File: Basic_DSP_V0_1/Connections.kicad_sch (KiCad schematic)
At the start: 40 parts, among them J10 53048-0310, J13 USB_C_Receptacle, J14 53048-0210, J15 53048-0210, J16 Conn_02x08_Odd_Even, J2 53048-0310, J3 53048-0310, J7 53048-0310, J8 53048-0310, J9 53048-0310

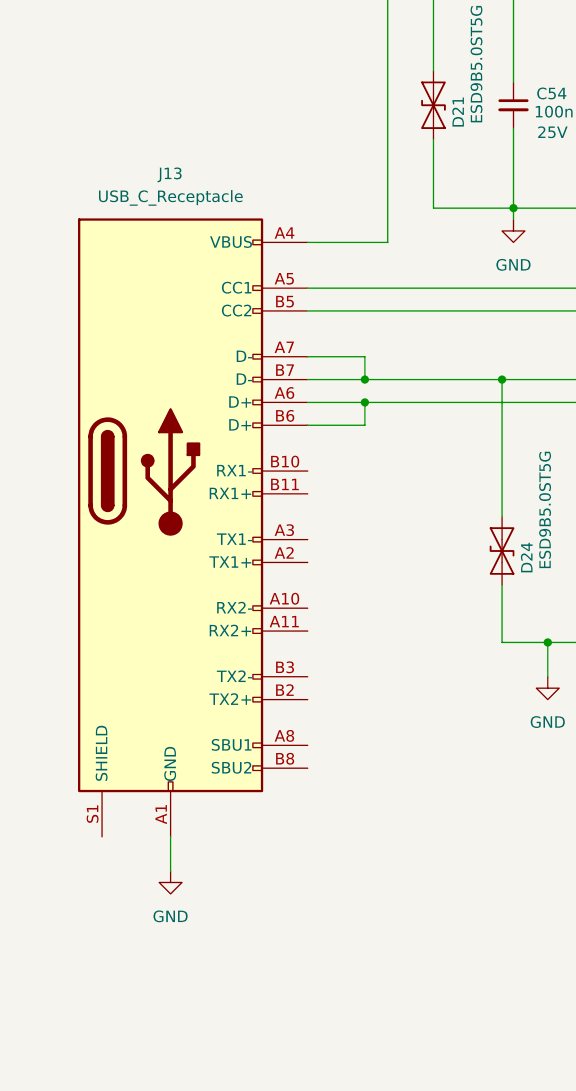
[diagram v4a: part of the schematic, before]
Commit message: More layout on Basic_DSP_V0_1 and a change of USB connector
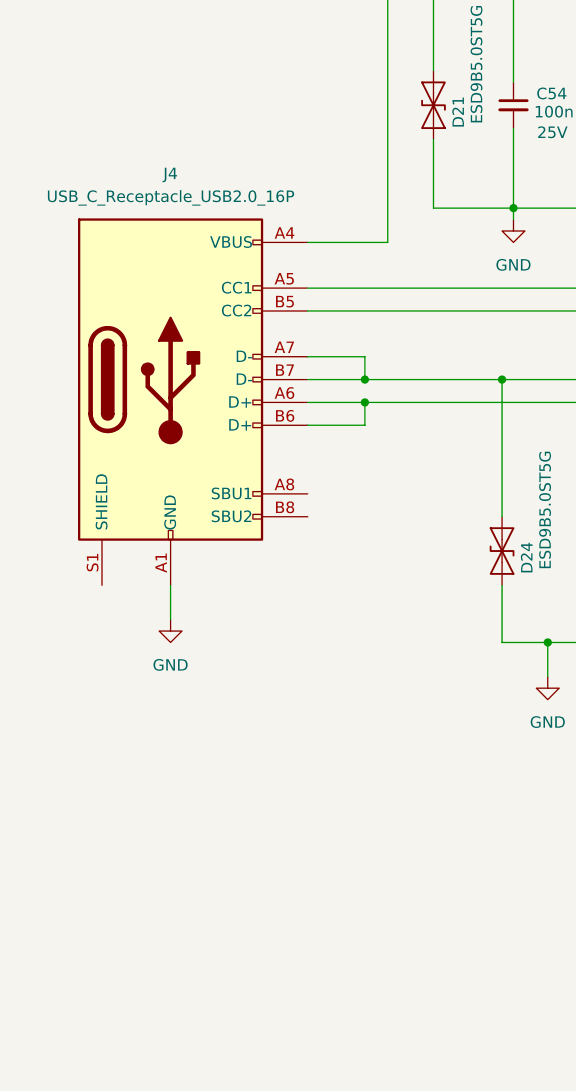
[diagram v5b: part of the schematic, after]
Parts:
- removed J13: USB_C_Receptacle, Connector_USB:USB_C_Receptacle_Molex_105450-0101, symbol Connector:USB_C_Receptacle
- added J4: USB_C_Receptacle_USB2.0_16P, Connector_USB:USB_C_Receptacle_GCT_USB4085, symbol Connector:USB_C_Receptacle_USB2.0_16P
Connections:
- net GND: now also J4.A1 (GND), J4.A12 (GND), J4.B1 (GND), J4.B12 (GND)
- net USB_D+: now also J4.A6 (D+), J4.B6 (D+)
- net USB_D-: now also J4.A7 (D-), J4.B7 (D-)
- net VBUS: now also J4.A4 (VBUS), J4.A9 (VBUS), J4.B4 (VBUS), J4.B9 (VBUS)
- net at R40.2: now also J4.A5 (CC1)
- net at R39.2: now also J4.B5 (CC2)
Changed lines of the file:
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@@
 	(wire
 		(pts
-			(xy 104.14 170.18) (xy 104.14 173.99)
+			(xy 104.14 142.24) (xy 104.14 146.05)
 		)
 		(stroke
@@
 	)
 	(symbol
+		(lib_id "Connector:USB_C_Receptacle_USB2.0_16P")
+		(at 104.14 119.38 0)
+		(unit 1)
+		(exclude_from_sim no)
+		(in_bom yes)
+		(on_board yes)
+		(dnp no)
+		(fields_autoplaced yes)
+		(property "Reference" "J4"
+			(at 104.14 96.52 0)
+			(effects
+				(font
+					(size 1.27 1.27)
+				)
+			)
+		)
+		(property "Value" "USB_C_Receptacle_USB2.0_16P"
+			(at 104.14 99.06 0)
+			(effects
+				(font
+					(size 1.27 1.27)
+				)
+			)
+		)
+		(property "Footprint" "Connector_USB:USB_C_Receptacle_GCT_USB4085"
+			(at 107.95 119.38 0)
+			(effects
+				(font
+					(size 1.27 1.27)
+				)
+				(hide yes)
+			)
+		)
+		(property "Datasheet" "https://www.usb.org/sites/default/files/documents/usb_type-c.zip"
+			(at 107.95 119.38 0)
+			(effects
+				(font
+					(size 1.27 1.27)
+				)
+				(hide yes)
+			)
+		)
+		(property "Description" "USB 2.0-only 16P Type-C Receptacle connector"
+			(at 104.14 119.38 0)
+			(effects
+				(font
+					(size 1.27 1.27)
+				)
+				(hide yes)
+			)
+		)
+		(pin "A4"
+		)
+		(pin "B7"
+		)
+		(pin "A12"
+		)
+		(pin "A7"
+		)
+		(pin "B5"
+		)
+		(pin "B8"
+		)
+		(pin "A8"
+		)
+		(pin "A9"
+		)
+		(pin "A5"
+		)
+		(pin "A1"
+		)
+		(pin "B12"
+		)
+		(pin "B4"
+		)
+		(pin "S1"
+		)
+		(pin "B1"
+		)
+		(pin "B6"
+		)
+		(pin "B9"
+		)
+		(pin "A6"
+		)
+		(instances
+			(project ""
+				(path "/b632011b-bebd-450c-b21c-a571983f756a/a6a37837-a89c-47bf-8760-dcad102ca010"
+					(reference "J4")
+					(unit 1)
+				)
+			)
+		)
+	)
+	(symbol
 		(lib_id "Chase_Conn:53048-0310")
 		(at 527.05 92.71 0)
@@
 	)
 	(symbol
-		(lib_id "Connector:USB_C_Receptacle")
-		(at 104.14 129.54 0)
-		(unit 1)
-		(exclude_from_sim no)
-		(in_bom yes)
-		(on_board yes)
-		(dnp no)
-		(fields_autoplaced yes)
-		(property "Reference" "J13"
-			(at 104.14 96.52 0)
-			(effects
-				(font
-					(size 1.27 1.27)
-				)
-			)
-		)
-		(property "Value" "USB_C_Receptacle"
-			(at 104.14 99.06 0)
-			(effects
-				(font
-					(size 1.27 1.27)
-				)
-			)
-		)
-		(property "Footprint" "Connector_USB:USB_C_Receptacle_Molex_105450-0101"
-			(at 107.95 129.54 0)
-			(effects
-				(font
-					(size 1.27 1.27)
-				)
-				(hide yes)
-			)
-		)
-		(property "Datasheet" "https://www.usb.org/sites/default/files/documents/usb_type-c.zip"
-			(at 107.95 129.54 0)
-			(effects
-				(font
-					(size 1.27 1.27)
-				)
-				(hide yes)
-			)
-		)
-		(property "Description" "USB Full-Featured Type-C Receptacle connector"
-			(at 104.14 129.54 0)
-			(effects
-				(font
-					(size 1.27 1.27)
-				)
-				(hide yes)
-			)
-		)
-		(property "OC_LCSC" "C134092"
-			(at 104.14 129.54 0)
-			(effects
-				(font
-					(size 1.27 1.27)
-				)
-				(hide yes)
-			)
-		)
-		(property "MF" "MOLEX"
-			(at 104.14 129.54 0)
-			(effects
-				(font
-					(size 1.27 1.27)
-				)
-				(hide yes)
-			)
-		)
-		(property "MPN" "  1054500101"
-			(at 104.14 129.54 0)
-			(effects
-				(font
-					(size 1.27 1.27)
-				)
-				(hide yes)
-			)
-		)
-		(pin "A4"
-		)
-		(pin "A6"
-		)
-		(pin "B9"
-		)
-		(pin "A10"
-		)
-		(pin "B4"
-		)
-		(pin "B5"
-		)
-		(pin "B8"
-		)
-		(pin "A7"
-		)
-		(pin "B10"
-		)
-		(pin "B12"
-		)
-		(pin "S1"
-		)
-		(pin "B6"
-		)
-		(pin "A5"
-		)
-		(pin "A9"
-		)
-		(pin "A3"
-		)
-		(pin "A8"
-		)
-		(pin "B11"
-		)
-		(pin "B3"
-		)
-		(pin "A2"
-		)
-		(pin "B2"
-		)
-		(pin "A12"
-		)
-		(pin "A1"
-		)
-		(pin "B7"
-		)
-		(pin "A11"
-		)
-		(pin "B1"
-		)
-		(instances
-			(project "Basic_DSP_V0_1"
-				(path "/b632011b-bebd-450c-b21c-a571983f756a/a6a37837-a89c-47bf-8760-dcad102ca010"
-					(reference "J13")
-					(unit 1)
-				)
-			)
-		)
-	)
-	(symbol
 		(lib_id "power:GND")
 		(at 106.68 346.71 0)
@@
 	(symbol
 		(lib_id "power:GND")
-		(at 104.14 173.99 0)
+		(at 104.14 146.05 0)
 		(unit 1)
 		(exclude_from_sim no)
@@
 		(fields_autoplaced yes)
 		(property "Reference" "#PWR075"
-			(at 104.14 180.34 0)
+			(at 104.14 152.4 0)
 			(effects
 				(font
@@
 		)
 		(property "Value" "GND"
-			(at 104.14 179.07 0)
+			(at 104.14 151.13 0)
 			(effects
 				(font
@@
 		)
 		(property "Footprint" ""
-			(at 104.14 173.99 0)
+			(at 104.14 146.05 0)
 			(effects
 				(font
@@
 		)
 		(property "Datasheet" ""
-			(at 104.14 173.99 0)
+			(at 104.14 146.05 0)
 			(effects
 				(font
@@
 		)
 		(property "Description" "Power symbol creates a global label with name \"GND\" , ground"
-			(at 104.14 173.99 0)
+			(at 104.14 146.05 0)
 			(effects
 				(font

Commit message: More layout work
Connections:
- net VBUS_FILT: now reaches C55.1, FB2.2
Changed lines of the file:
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@@
 	)
 	(junction
+		(at 165.1 74.93)
+		(diameter 0)
+		(color 0 0 0 0)
+	)
+	(junction
 		(at 495.3 165.1)
 		(diameter 0)
@@
 	(wire
 		(pts
+			(xy 165.1 66.04) (xy 165.1 74.93)
+		)
+		(stroke
+			(width 0)
+			(type default)
+		)
+	)
+	(wire
+		(pts
 			(xy 387.35 59.69) (xy 387.35 67.31)
 		)
@@
 					(unit 1)
 				)
+			)
+		)
+	)
+	(symbol
+		(lib_id "power:VBUS")
+		(at 165.1 66.04 0)
+		(unit 1)
+		(exclude_from_sim no)
+		(in_bom yes)
+		(on_board yes)
+		(dnp no)
+		(fields_autoplaced yes)
+		(property "Reference" "#PWR028"
+			(at 165.1 69.85 0)
+			(effects
+				(font
+					(size 1.27 1.27)
+				)
+				(hide yes)
+			)
+		)
+		(property "Value" "VBUS_FILT"
+			(at 165.1 60.96 0)
+			(effects
+				(font
+					(size 1.27 1.27)
+				)
+			)
+		)
+		(property "Footprint" ""
+			(at 165.1 66.04 0)
+			(effects
+				(font
+					(size 1.27 1.27)
+				)
+				(hide yes)
+			)
+		)
+		(property "Datasheet" ""
+			(at 165.1 66.04 0)
+			(effects
+				(font
+					(size 1.27 1.27)
+				)
+				(hide yes)
+			)
+		)
+		(property "Description" "Power symbol creates a global label with name \"VBUS\""
+			(at 165.1 66.04 0)
+			(effects
+				(font
+					(size 1.27 1.27)
+				)
+				(hide yes)
+			)
+		)
+		(pin "1"
+		)
+		(instances
+			(project "Basic_DSP_V0_1"
+				(path "/b632011b-bebd-450c-b21c-a571983f756a/a6a37837-a89c-47bf-8760-dcad102ca010"
+					(reference "#PWR028")
+					(unit 1)
+				)

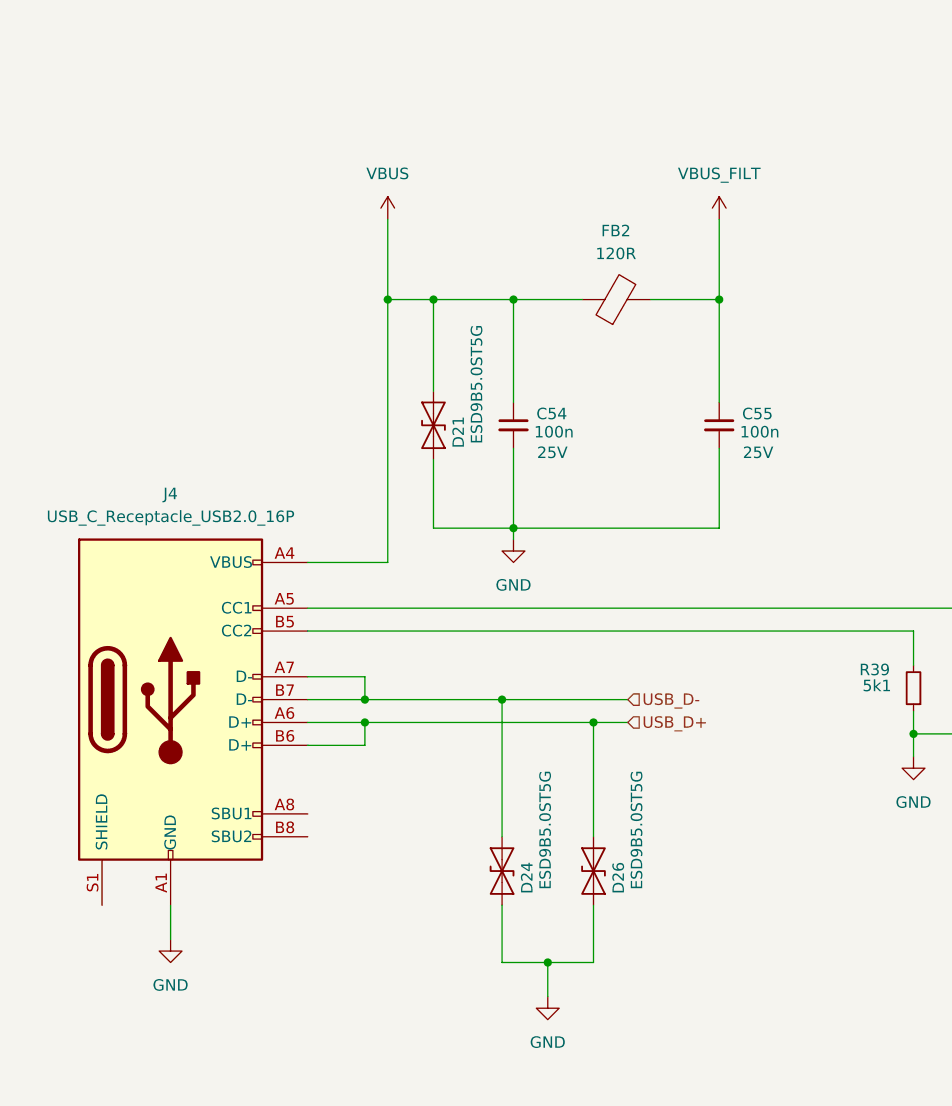
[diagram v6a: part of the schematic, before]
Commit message: Layout and removal of PDN ferrites
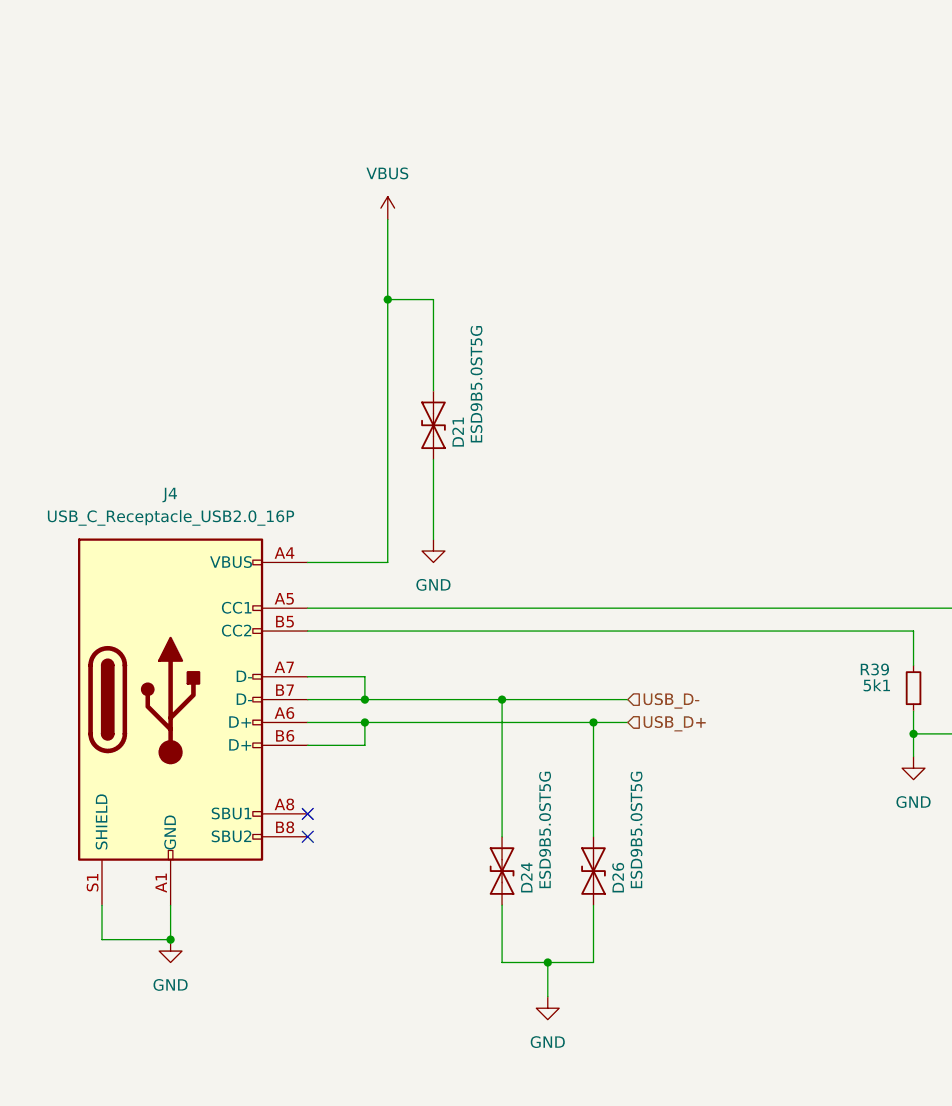
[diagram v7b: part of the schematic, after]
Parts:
- removed C54, C55: 100n, Capacitor_SMD:C_0603_1608Metric_Pad1.08x0.95mm_HandSolder, symbol Device:C_Small
- removed FB2: 120R, Inductor_SMD:L_0603_1608Metric, symbol Device:FerriteBead
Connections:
- net GND: now also J4.S1 (SHIELD)
- no-connect marks 0 -> 2

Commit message: No errors from DRC on layout
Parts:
- J4: footprint Connector_USB:USB_C_Receptacle_GCT_USB4085 -> Connector_USB:USB_C_Receptacle_GCT_USB4110
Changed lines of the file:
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@@
 			)
 		)
-		(property "Footprint" "Connector_USB:USB_C_Receptacle_GCT_USB4085"
+		(property "Footprint" "Connector_USB:USB_C_Receptacle_GCT_USB4110"
 			(at 107.95 119.38 0)
 			(effects
